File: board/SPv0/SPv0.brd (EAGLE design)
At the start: 96.8 x 31.8 mm, 53 parts, among them IC1 S34ML0XG1, IC2 F55[0/1]X---PT48, IC3 LM339D, Q1 12MHz, T1 n3904, T2 n3904, T3 n3906, T4 n3906, T5 n3906

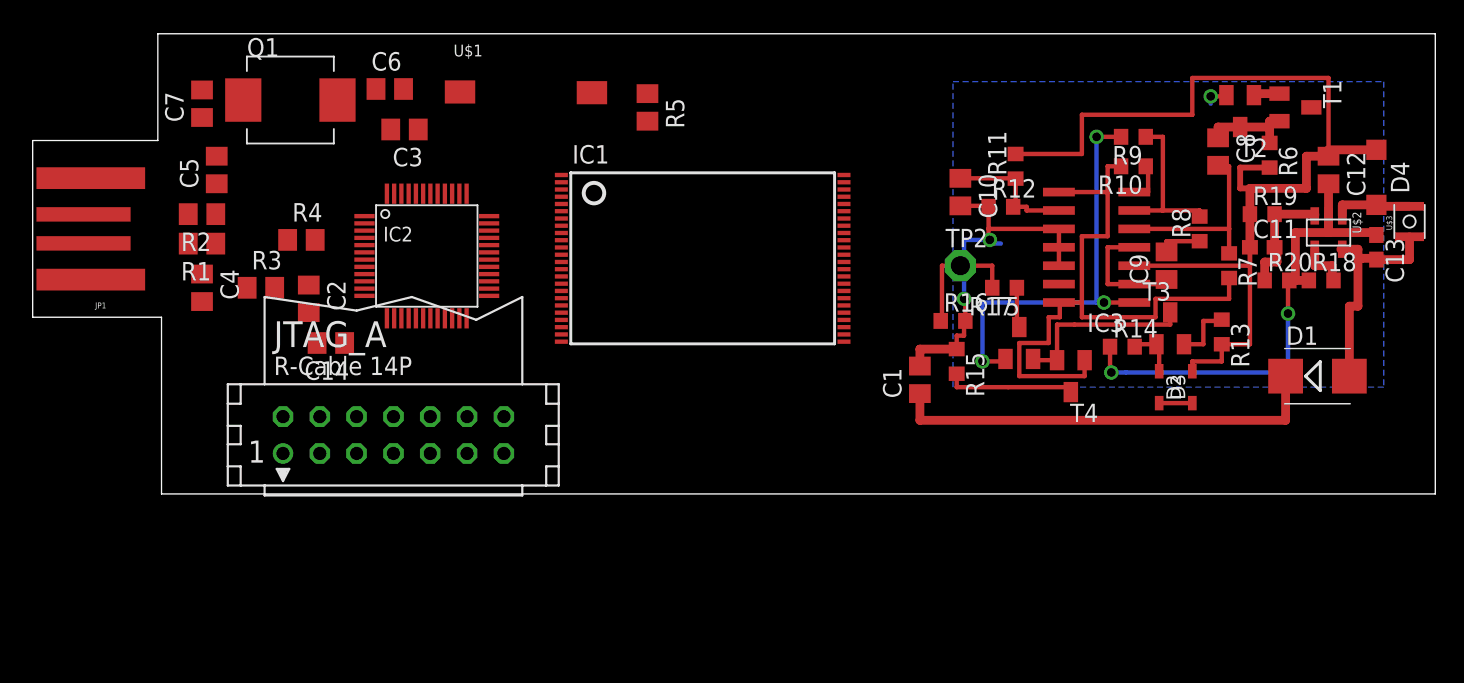
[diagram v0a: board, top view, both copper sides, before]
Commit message: fix dru errors
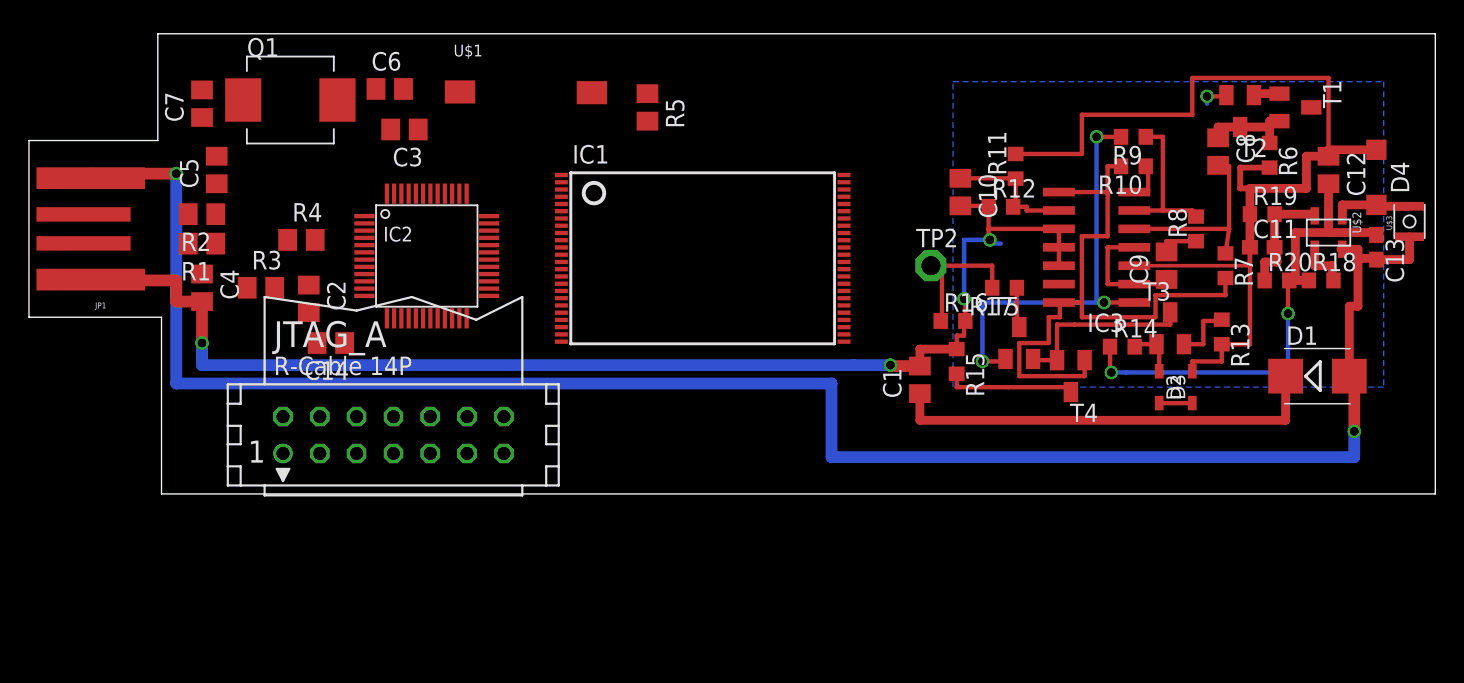
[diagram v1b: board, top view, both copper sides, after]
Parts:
- moved TP2 2.03 mm to (61.7, 17.5)
- moved R7 0.25 mm to (82.0, 17.5)
- moved R8 0.25 mm to (80.0, 20.1)
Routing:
- net VCC: track 16.0 -> 129.0 mm, vias 0 -> 2
- net GND: track 63.6 -> 127.0 mm, vias 5 -> 7
- net DOUT: track 8.89 -> 10.4 mm
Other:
- board size 96.8 x 31.8 mm -> 97 x 31.8 mm

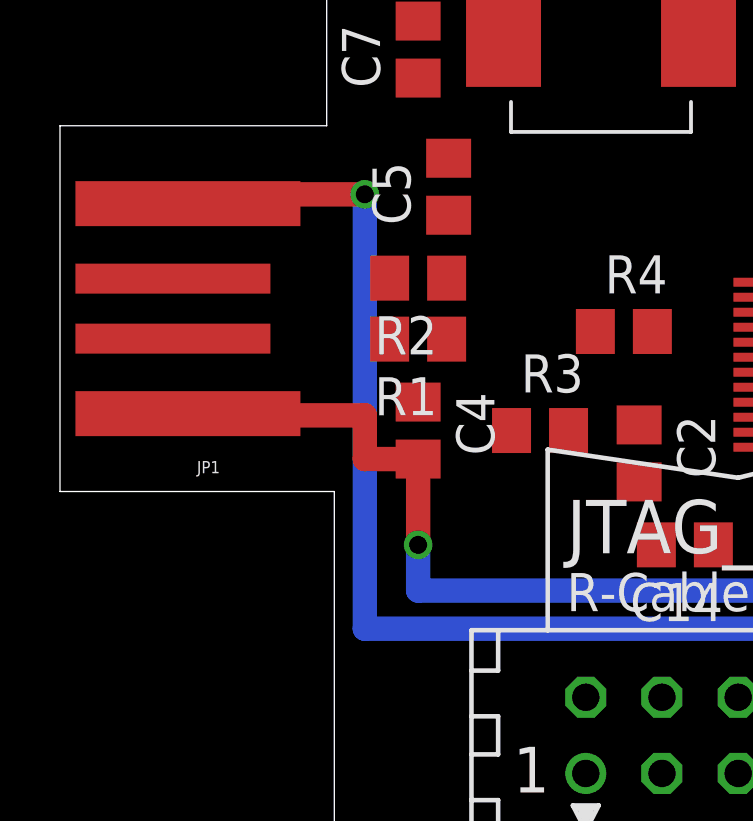
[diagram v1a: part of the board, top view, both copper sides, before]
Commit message: fixup usb problems
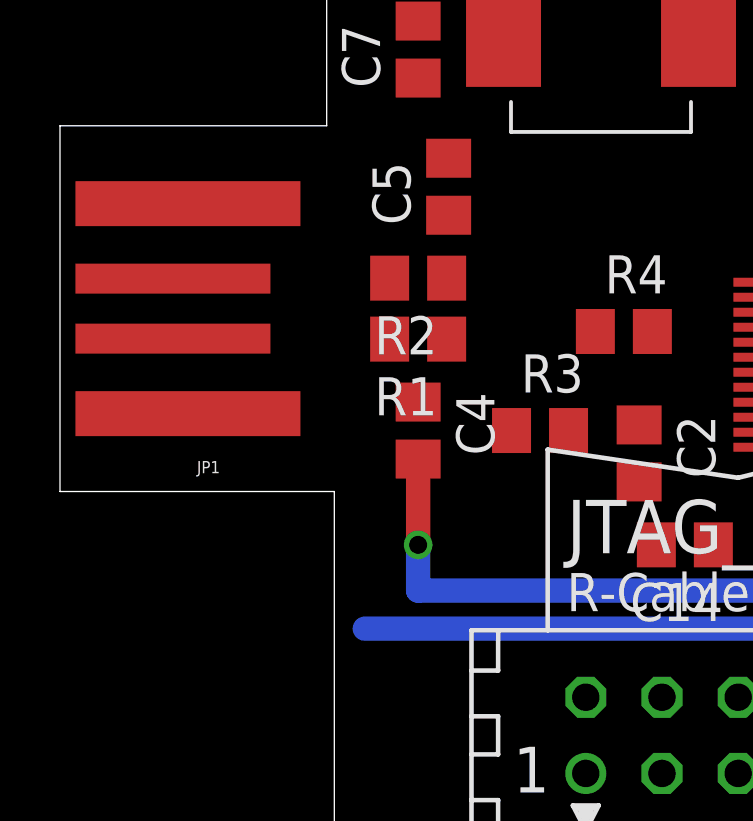
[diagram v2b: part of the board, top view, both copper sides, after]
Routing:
- net VCC: track 129.0 -> 108.3 mm, vias 2 -> 1
- net GND: track 127.0 -> 117.8 mm
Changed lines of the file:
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@@
 <wire x1="60.96" y1="10.602" x2="60.96" y2="11.772" width="0.6096" layer="1"/>
 <wire x1="60.96" y1="11.772" x2="63.5" y2="11.772" width="0.6096" layer="1"/>
-<wire x1="3.756" y1="16.566" x2="3.756" y2="16.51" width="0.8128" layer="1"/>
-<wire x1="3.756" y1="16.51" x2="9.652" y2="16.51" width="0.8128" layer="1"/>
-<wire x1="9.652" y1="16.51" x2="9.652" y2="15.052" width="0.8128" layer="1"/>
-<wire x1="9.652" y1="15.052" x2="11.43" y2="15.052" width="0.8128" layer="1"/>
 <wire x1="11.43" y1="15.052" x2="11.43" y2="12.192" width="0.8128" layer="1"/>
 <via x="11.43" y="12.192" extent="1-16" drill="0.6"/>
@@
 <wire x1="58.928" y1="10.668" x2="58.928" y2="10.602" width="0.8128" layer="1"/>
 <wire x1="58.928" y1="10.602" x2="60.96" y2="10.602" width="0.8128" layer="1"/>
-<wire x1="89.154" y1="23.18" x2="82.108" y2="29.21" width="0" layer="19" extent="1-1"/>
-<wire x1="70.552" y1="17.526" x2="74.08" y2="11.938" width="0" layer="19" extent="1-1"/>
-<wire x1="55.724" y1="12.284" x2="56.388" y2="10.668" width="0" layer="19" extent="1-16"/>
+<wire x1="56.388" y1="10.668" x2="55.724" y2="12.284" width="0" layer="19" extent="1-16"/>
 <wire x1="14.544" y1="16.002" x2="11.43" y2="15.052" width="0" layer="19" extent="1-1"/>
 <wire x1="18.796" y1="14.29" x2="14.544" y2="16.002" width="0" layer="19" extent="1-1"/>
@@
 <wire x1="24.45" y1="26.924" x2="26.18676875" y2="22.495553125" width="0" layer="19" extent="1-1"/>
 <wire x1="23.434" y1="29.718" x2="24.45" y2="26.924" width="0" layer="19" extent="1-1"/>
-<wire x1="12.446" y1="25.08" x2="9.652" y2="16.51" width="0" layer="19" extent="1-1"/>
+<wire x1="12.446" y1="25.08" x2="14.544" y2="16.002" width="0" layer="19" extent="1-1"/>
 <wire x1="11.43" y1="27.752" x2="12.446" y2="25.08" width="0" layer="19" extent="1-1"/>
+<wire x1="3.756" y1="23.566" x2="11.43" y2="27.752" width="0" layer="19" extent="1-1"/>
 <wire x1="27.178" y1="4.572" x2="19.37" y2="12.192" width="0" layer="19" extent="1-1"/>
 </signal>
@@
 <wire x1="91.186" y1="14.732" x2="91.186" y2="18.034" width="0.6096" layer="1"/>
 <wire x1="91.186" y1="18.034" x2="91.44" y2="18.034" width="0.6096" layer="1"/>
-<wire x1="3.756" y1="23.566" x2="3.756" y2="23.876" width="0.8128" layer="1"/>
-<wire x1="3.756" y1="23.876" x2="9.652" y2="23.876" width="0.8128" layer="1"/>
-<via x="9.652" y="23.876" extent="1-16" drill="0.6"/>
-<wire x1="9.652" y1="23.876" x2="9.652" y2="9.398" width="0.8128" layer="16"/>
 <wire x1="9.652" y1="9.398" x2="54.864" y2="9.398" width="0.8128" layer="16"/>
 <wire x1="54.864" y1="9.398" x2="54.864" y2="4.318" width="0.8128" layer="16"/>
@@
 <wire x1="90.932" y1="6.096" x2="90.932" y2="9.906" width="0.8128" layer="1"/>
 <wire x1="90.932" y1="9.906" x2="90.592" y2="9.906" width="0.8128" layer="1"/>
+<wire x1="9.652" y1="9.398" x2="3.756" y2="16.566" width="0" layer="19" extent="1-16"/>
 </signal>
 <signal name="N$5">
@@
 <wire x1="62.484" y1="17.526" x2="62.484" y2="13.716" width="0.3048" layer="1"/>
 <wire x1="62.484" y1="13.716" x2="62.396" y2="13.716" width="0.3048" layer="1"/>
-<wire x1="22.63676875" y1="20.945553125" x2="62.484" y2="17.526" width="0" layer="19" extent="1-1"/>
+<wire x1="22.63676875" y1="20.945553125" x2="61.722" y2="17.526" width="0" layer="19" extent="1-1"/>
 </signal>
 <signal name="VDD">

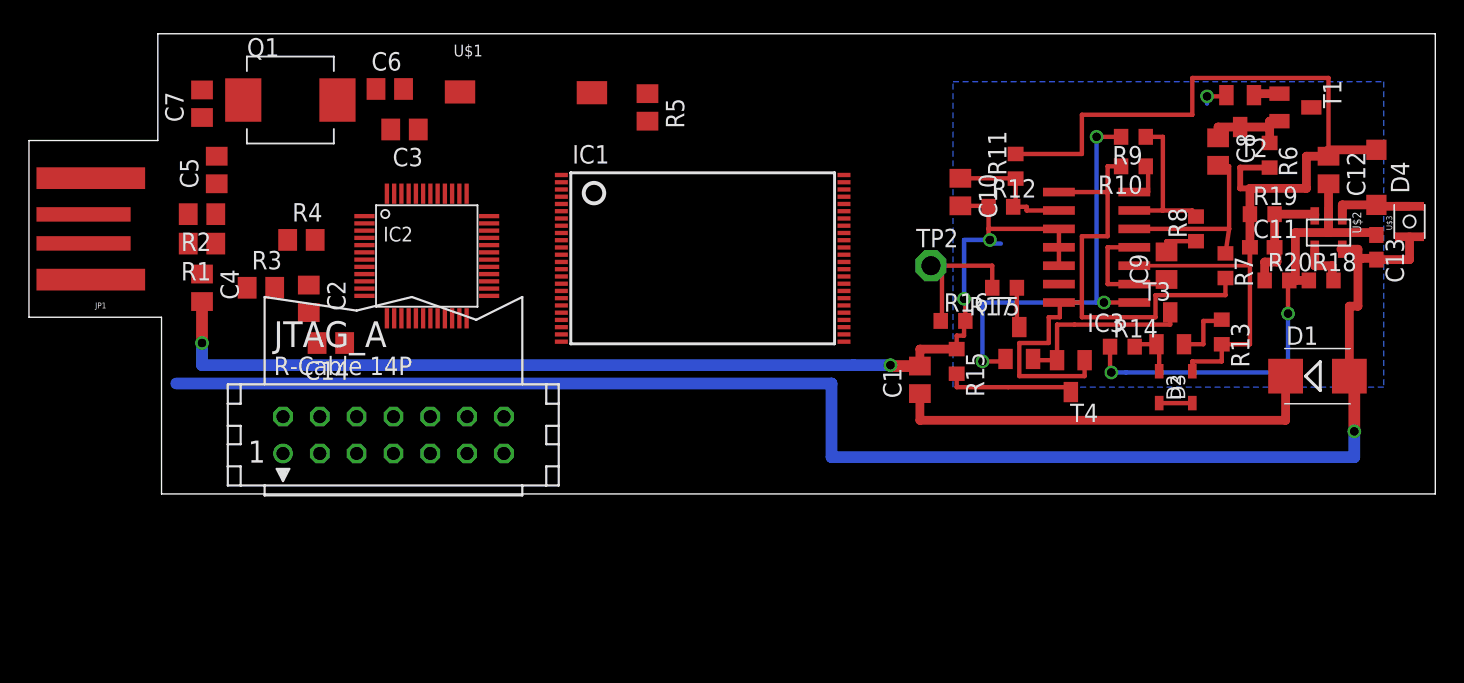
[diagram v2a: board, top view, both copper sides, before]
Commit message: added own footprints for 0805 parts reorganizing board somewhat
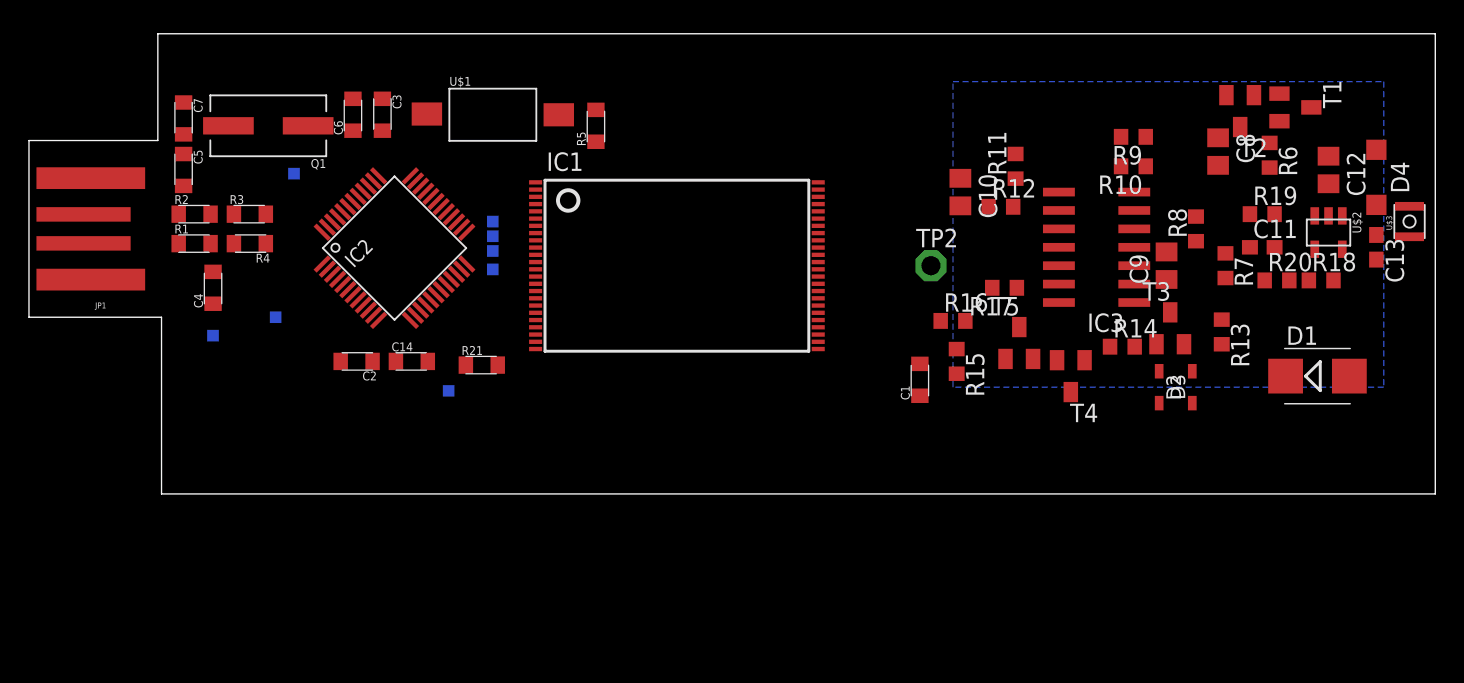
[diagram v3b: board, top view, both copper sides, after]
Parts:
- removed JTAG_A: (no value), con-harting:CON14
- added R21: 1M, Passives:R0805
- added TP1, TP3, TP4, TP5, TP6, TP7, TP8, TP9: TPTP08SQ, testpad:TP08SQ
- C1, C14, C2, C3, C4, C5, C6, C7: device rcl:C0805 -> Passives:R0805
- Q1: device Passives:NX8045GB -> Passives:CSM-3X
- R1, R2, R3, R4, R5: device rcl:R0805 -> Passives:R0805
- moved C14 5.73 mm to (25.9, 10.9), turned to 0 degrees
- moved C2 5.44 mm to (22.1, 10.9), turned to 180 degrees
- moved R3 5.14 mm to (14.7, 21.1)
- moved R5 3.78 mm to (38.6, 27.2), turned to 90 degrees
- moved R4 3.57 mm to (14.7, 19.1), turned to 180 degrees
- moved C6 3.10 mm to (21.8, 27.9), turned to 90 degrees
- moved U$1 2.75 mm to (31.5, 27.9)
- moved Q1 2.34 mm to (16.0, 27.2), turned to 180 degrees
- moved IC2 2.29 mm to (24.7, 18.7), turned to 45 degrees
- moved C5 2.29 mm to (10.2, 24.1), turned to 270 degrees
- moved IC1 1.85 mm to (44.2, 17.5)
- moved C3 1.83 mm to (23.9, 27.9), turned to 270 degrees
- moved C7 1.63 mm to (10.2, 27.7), turned to 270 degrees
- moved C4 0.76 mm to (12.2, 16.0), turned to 90 degrees
- moved R1 0.51 mm to (10.9, 19.1), turned to 0 degrees
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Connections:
- net !RST_A!: now also R21.P$1, TP4.TP; no longer JTAG_A.11
- net +1V8_A: now also C3.P$1; no longer C3.1
- net +3V3_A: now also C2.P$1, R21.P$2, R5.P$2, TP3.TP; no longer C2.1, JTAG_A.2, R5.2
- net D+_A: now also C4.P$1, R1.P$1, R3.P$2, R4.P$1; no longer C4.1, R1.1, R3.2, R4.1
- net D-_A: now also C5.P$1, R2.P$1; no longer C5.1, R2.1
- net GND: now also C1.P$2, C14.P$2, C2.P$2, C3.P$2, C4.P$2, C5.P$2, C6.P$1, C7.P$1, R3.P$1, TP5.TP; no longer C1.2, C14.2, C2.2, C3.2, C4.2, C5.2, C6.1, C7.1, JTAG_A.9, R3.1
- net N$1: now also R1.P$2; no longer R1.2
- net N$2: now also R2.P$2; no longer R2.2
- net N$3: now also C14.P$1; no longer C14.1
- net N$4: now also R5.P$1; no longer R5.1
- net PUR_A: now also R4.P$2; no longer R4.2
- net TCK_A: now also TP6.TP; no longer JTAG_A.7
- net TDI_A: now also TP8.TP; no longer JTAG_A.3
- net TDO_A: now also TP9.TP; no longer JTAG_A.1
- net TMS_A: now also TP7.TP; no longer JTAG_A.5
- net TST_A: now also TP1.TP; no longer JTAG_A.8
- net VBUS: now also C1.P$1; no longer C1.1
- net XT2IN_A: now also C6.P$2; no longer C6.2
- net XT2OUT_A: now also C7.P$2; no longer C7.2
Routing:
- net GND: track 117.8 -> 0.00 mm, vias 7 -> 0
- net VCC: track 108.3 -> 0.00 mm, vias 1 -> 0
- net VDD: track 73.2 -> 0.00 mm
- net VREF: track 44.2 -> 0.00 mm
- net VBUS: track 30.1 -> 0.00 mm
- net AOUT: track 29.4 -> 0.00 mm, vias 3 -> 0
- net N$7: track 13.4 -> 0.00 mm
- net N$16: track 12.9 -> 0.00 mm
- net N$10: track 10.8 -> 0.00 mm
- net DOUT: track 10.4 -> 0.00 mm
- net N$12: track 9.35 -> 0.00 mm
- net N$17: track 9.14 -> 0.00 mm
- net N$8: track 8.76 -> 0.00 mm
- net N$21: track 8.48 -> 0.00 mm
- net N$5: track 6.56 -> 0.00 mm
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
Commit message: adding primordial hwrng support added leds to library, board
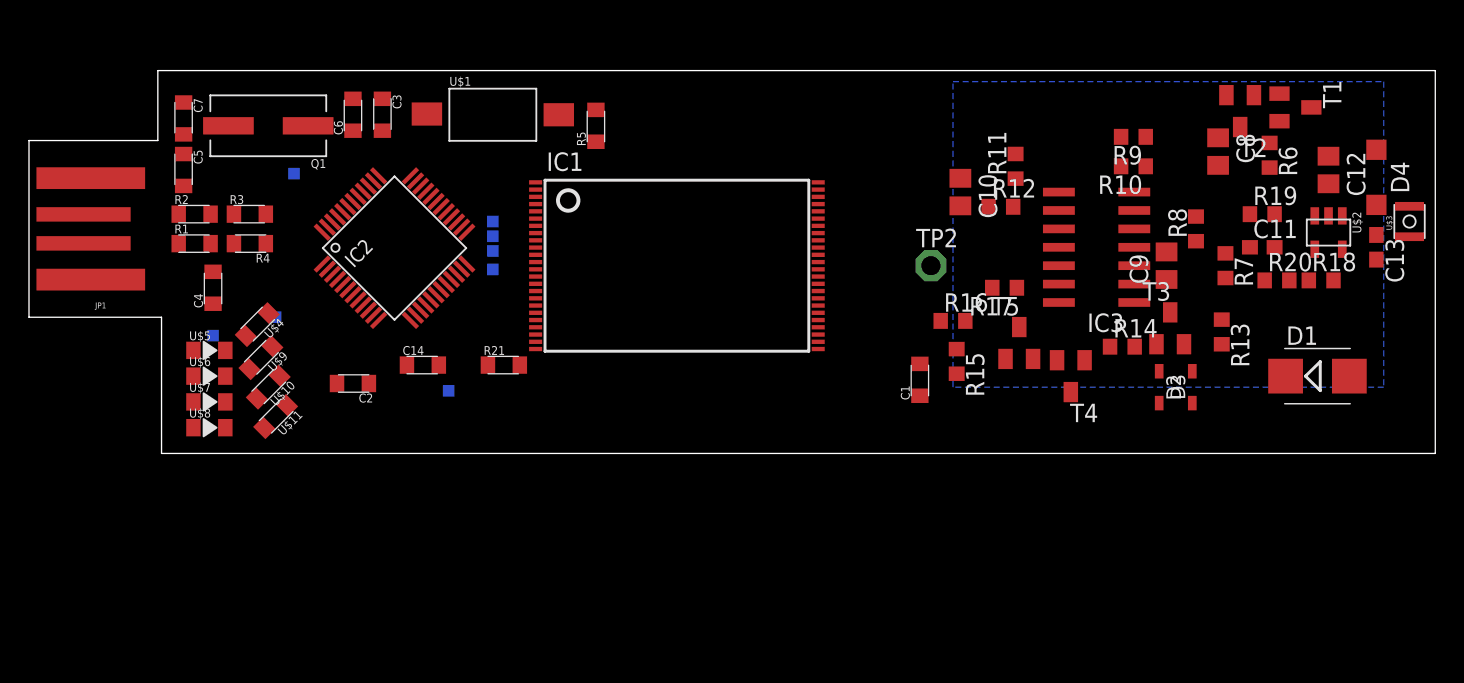
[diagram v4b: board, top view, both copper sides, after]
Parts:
- added U$10, U$11, U$4, U$9: R0805, Passives:R0805
- added U$5, U$6, U$7, U$8: LED, Passives:LED0805
- D2, D3: value (none) -> 1n4148
- IC3: value LM339D -> TL084D
- moved C2 1.55 mm to (21.8, 9.40)
- moved R21 1.52 mm to (32.3, 10.7)
- moved C14 0.80 mm to (26.7, 10.7)
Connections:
- new net N$19: IC2.9, U$11.P$2
- new net N$22: U$10.P$1, U$7.CATHODE
- new net N$23: U$6.CATHODE, U$9.P$1
- new net N$24: U$4.P$1, U$5.CATHODE
- new net N$25: U$11.P$1, U$8.CATHODE
- new net N$26: IC2.8, U$10.P$2
- new net N$27: IC2.6, U$9.P$2
- new net N$28: IC2.5, U$4.P$2
- net +3V3_A: now also U$5.ANODE, U$6.ANODE, U$7.ANODE, U$8.ANODE
- net AOUT: now also IC3.7; no longer IC3.1
- net GND: now also IC3.13; no longer IC3.10
- net N$11: now also IC3.5; no longer IC3.7
- net N$12: now also IC3.10; no longer IC3.9
- net N$7: now also IC3.3; no longer IC3.5
- net N$8: now also IC3.1; no longer IC3.4
- net VDD: now also IC3.4; no longer IC3.3
- net VREF: now also IC3.9; no longer IC3.14
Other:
- board size 97 x 31.8 mm -> 97 x 26.4 mm
